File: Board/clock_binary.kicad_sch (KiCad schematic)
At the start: 42 parts, among them U3 4081, U6 4040, U7 4040, U8 4040, U9 4082

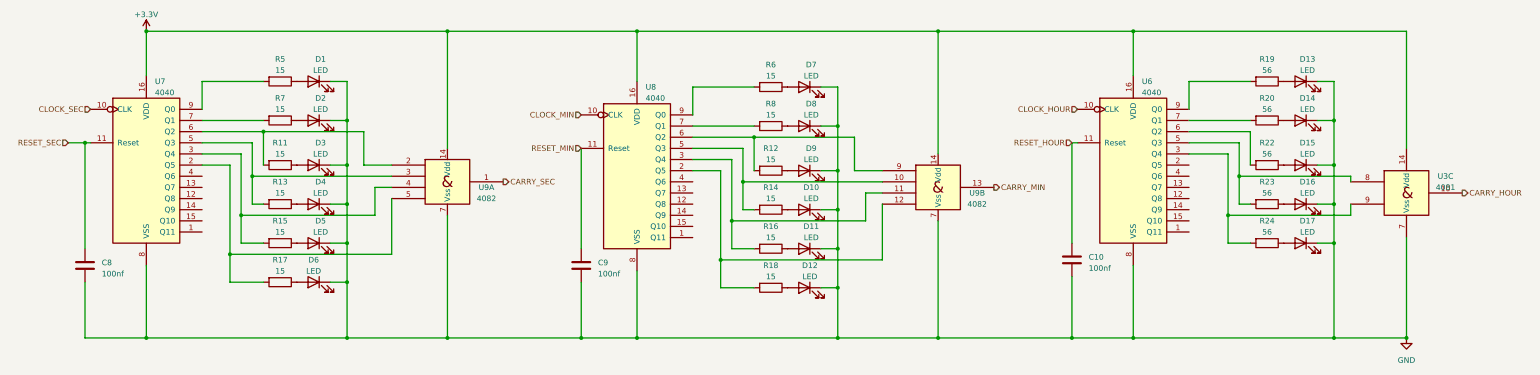
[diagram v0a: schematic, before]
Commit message: make power circuit from 120v mains
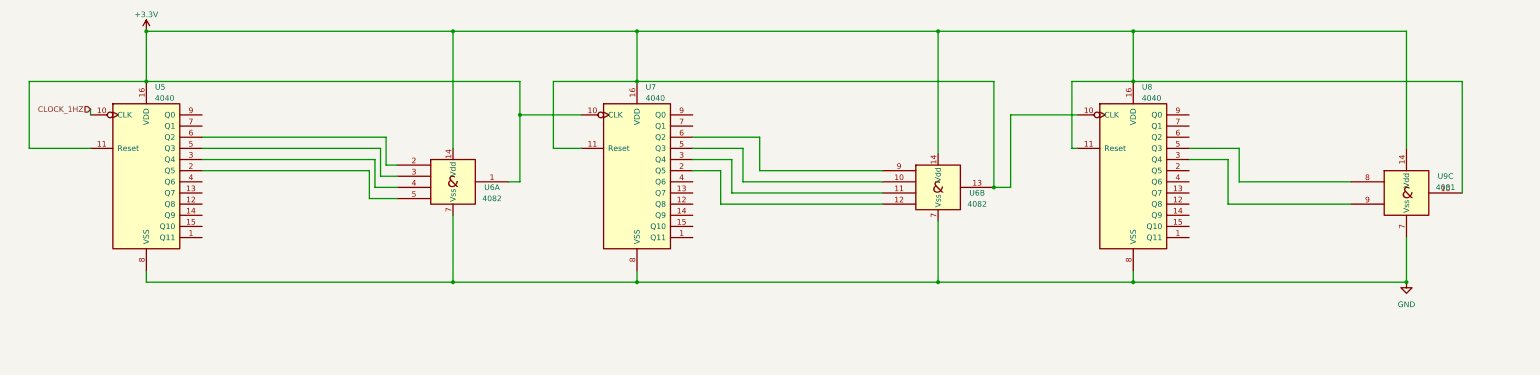
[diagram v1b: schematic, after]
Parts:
- removed C10, C8, C9: 100nf, Capacitor_THT:C_Disc_D5.1mm_W3.2mm_P5.00mm, symbol Device:C
- removed D1, D10, D11, D12, D13, D14, D15, D16, D17, D2, D3, D4, D5, D6, D7, D8, D9: LED, Connector_JST:JST_XH_B2B-XH-A_1x02_P2.50mm_Vertical, symbol Device:LED
- removed R11, R12, R13, R14, R15, R16, R17, R18, R5, R6, R7, R8: 15, Resistor_THT:R_Axial_DIN0204_L3.6mm_D1.6mm_P7.62mm_Horizontal, symbol Device:R
- removed R19, R20, R22, R23, R24: 56, Resistor_THT:R_Axial_DIN0204_L3.6mm_D1.6mm_P7.62mm_Horizontal, symbol Device:R
- renumbered U7 to U5, U9 to U6, U8 to U7, U6 to U8, U3 to U9
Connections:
- net CARRY_HOUR is gone; now on net +3.3V: U9.10
- net CARRY_MIN is gone; now on net +3.3V: U6.13
- net CARRY_SEC is gone; now on net +3.3V: U6.1
- net CLOCK_HOUR is gone; now on net +3.3V: U8.10 (CLK)
- net CLOCK_MIN is gone; now on net +3.3V: U7.10 (CLK)
- net RESET_HOUR is gone; now on net +3.3V: U8.11 (Reset)
- net RESET_MIN is gone; now on net +3.3V: U7.11 (Reset)
- net RESET_SEC is gone; now on net +3.3V: U5.11 (Reset)
- net CLOCK_SEC renamed CLOCK_1HZ
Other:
- moved on the sheet: U5, U6A, U8
